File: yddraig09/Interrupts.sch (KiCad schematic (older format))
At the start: 0 parts

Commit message: More work on 6809 board
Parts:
- added C? (x6): 100nF, symbol Device:C
- added RN?: 10K, Resistor_THT:R_Array_SIP9, symbol Device:R_Network08
- added U? (x4): 74LS11, symbol 74xx:74LS11
- added U? (x10): 74LS32, symbol 74xx:74LS32
- added U?: 74LS147, symbol 74xx:74LS147
- added U?: 74LS540, symbol 74xx:74LS540
- added U?: 74LS574, symbol 74xx:74LS574
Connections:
- new net: U?.1, U?.11 (E1), U?.3
- new net: U?.13, U?.8
- new net: U?.2, U?.6
- new net: U?.12 (E2), U?.3, U?.6
- new net: U?.13 (E3), U?.4, U?.8
- new net: U?.1 (E4), U?.11, U?.5
- new net: U?.10, U?.3 (E6), U?.6
- new net: U?.11, U?.4 (E7), U?.8
- new net: U?.2 (E5), U?.3, U?.9
- new net: U?.19 (Q0), U?.2
- new net: U?.18 (Q1), U?.5
- new net: U?.10, U?.17 (Q2)
- new net: U?.13, U?.16 (Q3)
- new net: U?.15 (Q4), U?.2
- new net: U?.14 (Q5), U?.5
- new net: U?.10, U?.13 (Q6)
- new net: U?.11, U?.11 (Cp)
- new net: U?.14 (S3), U?.5 (A3)
- new net: U?.4 (A2), U?.6 (S2)
- new net: U?.3 (A1), U?.7 (S1)
- new net: U?.2 (A0), U?.9 (S0)
- new net +5V: C?.1, C?.1, C?.1, C?.1, C?.1, C?.1, RN?.1 (common), U?.10 (E9), U?.14 (VCC), U?.14 (VCC), U?.14 (VCC), U?.16 (VCC), U?.20 (VCC), U?.20 (VCC), U?.5 (E8), U?.6 (A4), U?.7 (A5), U?.8 (A6), U?.9 (A7)
- new net D0: U?.18 (Y0), U?.2 (D0)
- new net D1: U?.17 (Y1), U?.3 (D1)
- new net D2: U?.16 (Y2), U?.4 (D2)
- new net D3: U?.15 (Y3), U?.5 (D3)
- new net D4: U?.14 (Y4), U?.6 (D4)
- new net D5: U?.13 (Y5), U?.7 (D5)
- new net D6: U?.12 (Y6), U?.8 (D6)
- new net D7: U?.11 (Y7), U?.9 (D7)
- new net GND: C?.2, C?.2, C?.2, C?.2, C?.2, C?.2, U?.1 (OE), U?.10 (GND), U?.10 (GND), U?.7 (GND), U?.7 (GND), U?.7 (GND), U?.8 (GND)
- new net ~CS_IRQEN: U?.12, U?.19 (G2)
- new net ~IRQ: U?.12
- new net ~IRQ0: RN?.2 (R1), U?.1
- new net ~IRQ1: RN?.3 (R2), U?.4
- new net ~IRQ2: RN?.4 (R3), U?.9
- new net ~IRQ3: RN?.5 (R4), U?.12
- new net ~IRQ4: RN?.6 (R5), U?.1
- new net ~IRQ5: RN?.7 (R6), U?.4
- new net ~IRQ6: RN?.8 (R7), U?.9
- new net ~RD: U?.1 (G1)
- new net ~WR: U?.13
- no-connect marks 0 -> 2

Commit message: ddraig09: initial design done
Need to be reviewed and decode on additional uses for IO but passed DRC
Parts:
- added C801, C802, C803, C804, C805, C806: 100nF, symbol Device:C
- gave numbers to parts that had none: 13
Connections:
- net +5V: now also C801.1, C802.1, C803.1, C804.1, C805.1, C806.1
- net GND: now also C801.2, C802.2, C803.2, C804.2, C805.2, C806.2

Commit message: Asssigned part footprints to most of schematic
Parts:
- C801, C802, C803, C804, C805, C806, C807, C808, C809, C810, C811, C812: footprint (none) -> Capacitor_THT:C_Disc_D5.0mm_W2.5mm_P2.50mm
- U801, U803, U804: footprint (none) -> Package_DIP:DIP-14_W7.62mm_Socket
- U802, U806: footprint (none) -> Package_DIP:DIP-20_W7.62mm_Socket
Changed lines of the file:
@@
 F 0 "U804" H 9300 1450 50  0000 C CNN
 F 1 "74LS11" H 9700 1450 50  0000 C CNN
-F 2 "" H 9500 1200 50  0001 C CNN
+F 2 "Package_DIP:DIP-14_W7.62mm_Socket" H 9500 1200 50  0001 C CNN
 F 3 "http://www.ti.com/lit/gpn/sn74LS11" H 9500 1200 50  0001 C CNN
 	1    9500 1200
@@
 F 0 "U804" H 8350 1850 50  0000 C CNN
 F 1 "74LS11" H 8800 1850 50  0000 C CNN
-F 2 "" H 8550 1600 50  0001 C CNN
+F 2 "Package_DIP:DIP-14_W7.62mm_Socket" H 8550 1600 50  0001 C CNN
 F 3 "http://www.ti.com/lit/gpn/sn74LS11" H 8550 1600 50  0001 C CNN
 	2    8550 1600
@@
 F 0 "U804" H 8350 2400 50  0000 C CNN
 F 1 "74LS11" H 8800 2400 50  0000 C CNN
-F 2 "" H 8550 2150 50  0001 C CNN
+F 2 "Package_DIP:DIP-14_W7.62mm_Socket" H 8550 2150 50  0001 C CNN
 F 3 "http://www.ti.com/lit/gpn/sn74LS11" H 8550 2150 50  0001 C CNN
 	3    8550 2150
@@
 F 0 "U804" H 10700 6600 50  0000 L CNN
 F 1 "74LS11" H 10700 5900 50  0000 L CNN
-F 2 "" H 10650 6250 50  0001 C CNN
+F 2 "Package_DIP:DIP-14_W7.62mm_Socket" H 10650 6250 50  0001 C CNN
 F 3 "http://www.ti.com/lit/gpn/sn74LS11" H 10650 6250 50  0001 C CNN
 	4    10650 6250
@@
 F 0 "U801" H 5300 1750 50  0000 C CNN
 F 1 "74LS32" H 5700 1750 50  0000 C CNN
-F 2 "" H 5500 1500 50  0001 C CNN
+F 2 "Package_DIP:DIP-14_W7.62mm_Socket" H 5500 1500 50  0001 C CNN
 F 3 "http://www.ti.com/lit/gpn/sn74LS32" H 5500 1500 50  0001 C CNN
 	1    5500 1500
@@
 F 0 "U801" H 5300 2850 50  0000 C CNN
 F 1 "74LS32" H 5700 2850 50  0000 C CNN
-F 2 "" H 5500 2600 50  0001 C CNN
+F 2 "Package_DIP:DIP-14_W7.62mm_Socket" H 5500 2600 50  0001 C CNN
 F 3 "http://www.ti.com/lit/gpn/sn74LS32" H 5500 2600 50  0001 C CNN
 	3    5500 2600
@@
 F 0 "U803" H 5300 3400 50  0000 C CNN
 F 1 "74LS32" H 5700 3400 50  0000 C CNN
-F 2 "" H 5500 3150 50  0001 C CNN
+F 2 "Package_DIP:DIP-14_W7.62mm_Socket" H 5500 3150 50  0001 C CNN
 F 3 "http://www.ti.com/lit/gpn/sn74LS32" H 5500 3150 50  0001 C CNN
 	4    5500 3150
@@
 F 0 "U803" H 10050 6600 50  0000 L CNN
 F 1 "74LS32" H 10050 5900 50  0000 L CNN
-F 2 "" H 10000 6250 50  0001 C CNN
+F 2 "Package_DIP:DIP-14_W7.62mm_Socket" H 10000 6250 50  0001 C CNN
 F 3 "http://www.ti.com/lit/gpn/sn74LS32" H 10000 6250 50  0001 C CNN
 	5    10000 6250
@@
 F 0 "U803" H 5300 4000 50  0000 C CNN
 F 1 "74LS32" H 5700 4000 50  0000 C CNN
-F 2 "" H 5500 3750 50  0001 C CNN
+F 2 "Package_DIP:DIP-14_W7.62mm_Socket" H 5500 3750 50  0001 C CNN
 F 3 "http://www.ti.com/lit/gpn/sn74LS32" H 5500 3750 50  0001 C CNN
 	1    5500 3750
@@
 F 0 "U803" H 5300 4550 50  0000 C CNN
 F 1 "74LS32" H 5700 4550 50  0000 C CNN
-F 2 "" H 5500 4300 50  0001 C CNN
+F 2 "Package_DIP:DIP-14_W7.62mm_Socket" H 5500 4300 50  0001 C CNN
 F 3 "http://www.ti.com/lit/gpn/sn74LS32" H 5500 4300 50  0001 C CNN
 	2    5500 4300
@@
 F 0 "U803" H 5300 5100 50  0000 C CNN
 F 1 "74LS32" H 5700 5100 50  0000 C CNN
-F 2 "" H 5500 4850 50  0001 C CNN
+F 2 "Package_DIP:DIP-14_W7.62mm_Socket" H 5500 4850 50  0001 C CNN
 F 3 "http://www.ti.com/lit/gpn/sn74LS32" H 5500 4850 50  0001 C CNN
 	3    5500 4850
@@
 F 0 "U801" H 1850 6950 50  0000 C CNN
 F 1 "74LS32" H 2100 6500 50  0000 C CNN
-F 2 "" H 2050 6700 50  0001 C CNN
+F 2 "Package_DIP:DIP-14_W7.62mm_Socket" H 2050 6700 50  0001 C CNN
 F 3 "http://www.ti.com/lit/gpn/sn74LS32" H 2050 6700 50  0001 C CNN
 	4    2050 6700
@@
 F 0 "U801" H 9400 6600 50  0000 L CNN
 F 1 "74LS32" H 9400 5900 50  0000 L CNN
-F 2 "" H 9350 6250 50  0001 C CNN
+F 2 "Package_DIP:DIP-14_W7.62mm_Socket" H 9350 6250 50  0001 C CNN
 F 3 "http://www.ti.com/lit/gpn/sn74LS32" H 9350 6250 50  0001 C CNN
 	5    9350 6250
@@
 F 0 "U806" H 9650 4400 50  0000 C CNN
 F 1 "74LS540" H 10100 4400 50  0000 C CNN
-F 2 "" H 9900 3750 50  0001 C CNN
+F 2 "Package_DIP:DIP-20_W7.62mm_Socket" H 9900 3750 50  0001 C CNN
 F 3 "http://www.ti.com/lit/gpn/sn74LS540" H 9900 3750 50  0001 C CNN
 	1    9900 3750
@@
 F 0 "U802" H 3250 6950 50  0000 C CNN
 F 1 "74LS574" H 3700 6950 50  0000 C CNN
-F 2 "" H 3500 6300 50  0001 C CNN
+F 2 "Package_DIP:DIP-20_W7.62mm_Socket" H 3500 6300 50  0001 C CNN
 F 3 "http://www.ti.com/lit/gpn/sn74LS574" H 3500 6300 50  0001 C CNN
 	1    3500 6300
@@
 F 0 "U801" H 5300 2300 50  0000 C CNN
 F 1 "74LS32" H 5700 2300 50  0000 C CNN
-F 2 "" H 5500 2050 50  0001 C CNN
+F 2 "Package_DIP:DIP-14_W7.62mm_Socket" H 5500 2050 50  0001 C CNN
 F 3 "http://www.ti.com/lit/gpn/sn74LS32" H 5500 2050 50  0001 C CNN
 	2    5500 2050
@@
 F 0 "C807" H 6265 6296 50  0000 L CNN
 F 1 "100nF" H 6265 6205 50  0000 L CNN
-F 2 "" H 6188 6100 50  0001 C CNN
+F 2 "Capacitor_THT:C_Disc_D5.0mm_W2.5mm_P2.50mm" H 6188 6100 50  0001 C CNN
 F 3 "~" H 6150 6250 50  0001 C CNN
 	1    6150 6250
@@
 F 0 "C808" H 6765 6296 50  0000 L CNN
 F 1 "100nF" H 6765 6205 50  0000 L CNN
-F 2 "" H 6688 6100 50  0001 C CNN
+F 2 "Capacitor_THT:C_Disc_D5.0mm_W2.5mm_P2.50mm" H 6688 6100 50  0001 C CNN
 F 3 "~" H 6650 6250 50  0001 C CNN
 	1    6650 6250
@@
 F 0 "C809" H 7265 6296 50  0000 L CNN
 F 1 "100nF" H 7265 6205 50  0000 L CNN
-F 2 "" H 7188 6100 50  0001 C CNN
+F 2 "Capacitor_THT:C_Disc_D5.0mm_W2.5mm_P2.50mm" H 7188 6100 50  0001 C CNN
 F 3 "~" H 7150 6250 50  0001 C CNN
 	1    7150 6250
@@
 F 0 "C810" H 7765 6296 50  0000 L CNN
 F 1 "100nF" H 7765 6205 50  0000 L CNN
-F 2 "" H 7688 6100 50  0001 C CNN
+F 2 "Capacitor_THT:C_Disc_D5.0mm_W2.5mm_P2.50mm" H 7688 6100 50  0001 C CNN
 F 3 "~" H 7650 6250 50  0001 C CNN
 	1    7650 6250
@@
 F 0 "C811" H 8265 6296 50  0000 L CNN
 F 1 "100nF" H 8265 6205 50  0000 L CNN
-F 2 "" H 8188 6100 50  0001 C CNN
+F 2 "Capacitor_THT:C_Disc_D5.0mm_W2.5mm_P2.50mm" H 8188 6100 50  0001 C CNN
 F 3 "~" H 8150 6250 50  0001 C CNN
 	1    8150 6250
@@
 F 0 "C812" H 8765 6296 50  0000 L CNN
 F 1 "100nF" H 8765 6205 50  0000 L CNN
-F 2 "" H 8688 6100 50  0001 C CNN
+F 2 "Capacitor_THT:C_Disc_D5.0mm_W2.5mm_P2.50mm" H 8688 6100 50  0001 C CNN
 F 3 "~" H 8650 6250 50  0001 C CNN
 	1    8650 6250
@@
 F 0 "C801" H 1565 3246 50  0000 L CNN
 F 1 "100nF" H 1565 3155 50  0000 L CNN
-F 2 "" H 1488 3050 50  0001 C CNN
+F 2 "Capacitor_THT:C_Disc_D5.0mm_W2.5mm_P2.50mm" H 1488 3050 50  0001 C CNN
 F 3 "~" H 1450 3200 50  0001 C CNN
 	1    1450 3200
@@
 F 0 "C802" H 2065 3246 50  0000 L CNN
 F 1 "100nF" H 2065 3155 50  0000 L CNN
-F 2 "" H 1988 3050 50  0001 C CNN
+F 2 "Capacitor_THT:C_Disc_D5.0mm_W2.5mm_P2.50mm" H 1988 3050 50  0001 C CNN
 F 3 "~" H 1950 3200 50  0001 C CNN
 	1    1950 3200
@@
 F 0 "C804" H 2565 3246 50  0000 L CNN
 F 1 "100nF" H 2565 3155 50  0000 L CNN
-F 2 "" H 2488 3050 50  0001 C CNN
+F 2 "Capacitor_THT:C_Disc_D5.0mm_W2.5mm_P2.50mm" H 2488 3050 50  0001 C CNN
 F 3 "~" H 2450 3200 50  0001 C CNN
 	1    2450 3200
@@
 F 0 "C806" H 3065 3246 50  0000 L CNN
 F 1 "100nF" H 3065 3155 50  0000 L CNN
-F 2 "" H 2988 3050 50  0001 C CNN
+F 2 "Capacitor_THT:C_Disc_D5.0mm_W2.5mm_P2.50mm" H 2988 3050 50  0001 C CNN
 F 3 "~" H 2950 3200 50  0001 C CNN
 	1    2950 3200
@@
 F 0 "C803" H 2065 4396 50  0000 L CNN
 F 1 "100nF" H 2065 4305 50  0000 L CNN
-F 2 "" H 1988 4200 50  0001 C CNN
+F 2 "Capacitor_THT:C_Disc_D5.0mm_W2.5mm_P2.50mm" H 1988 4200 50  0001 C CNN
 F 3 "~" H 1950 4350 50  0001 C CNN
 	1    1950 4350
@@
 F 0 "C805" H 2565 4396 50  0000 L CNN
 F 1 "100nF" H 2565 4305 50  0000 L CNN
-F 2 "" H 2488 4200 50  0001 C CNN
+F 2 "Capacitor_THT:C_Disc_D5.0mm_W2.5mm_P2.50mm" H 2488 4200 50  0001 C CNN
 F 3 "~" H 2450 4350 50  0001 C CNN
 	1    2450 4350

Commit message: ddraig09: all footprints assigned
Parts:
- U805: footprint (none) -> Package_DIP:DIP-16_W7.62mm_Socket
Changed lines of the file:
@@
 F 0 "U805" H 8300 4200 50  0000 C CNN
 F 1 "74LS147" H 8750 4200 50  0000 C CNN
-F 2 "" H 8550 3650 50  0001 C CNN
+F 2 "Package_DIP:DIP-16_W7.62mm_Socket" H 8550 3650 50  0001 C CNN
 F 3 "http://www.ti.com/lit/gpn/sn74LS147" H 8550 3650 50  0001 C CNN
 	1    8550 3650

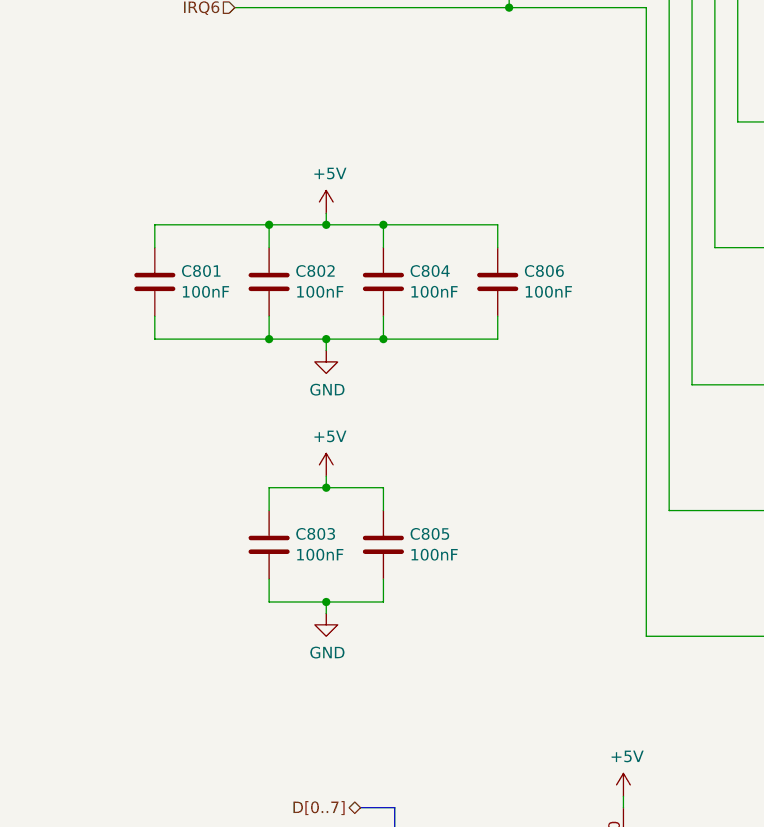
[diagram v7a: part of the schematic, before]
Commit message: Added initial 6809 board layout design
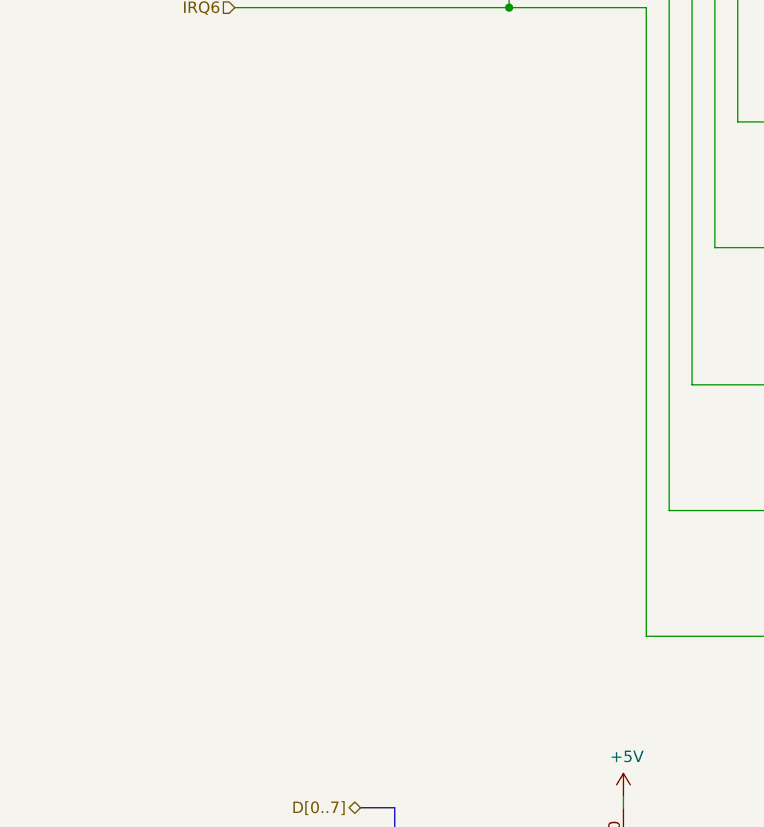
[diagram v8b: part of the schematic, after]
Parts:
- removed C801, C802, C803, C804, C805, C806: 100nF, Capacitor_THT:C_Disc_D5.0mm_W2.5mm_P2.50mm, symbol Device:C
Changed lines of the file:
@@
 Wire Bus Line
 	6950 4950 10850 4950
-$Comp
-L Device:C C801
-U 1 1 616F4D00
-P 1450 3200
-F 0 "C801" H 1565 3246 50  0000 L CNN
-F 1 "100nF" H 1565 3155 50  0000 L CNN
-F 2 "Capacitor_THT:C_Disc_D5.0mm_W2.5mm_P2.50mm" H 1488 3050 50  0001 C CNN
-F 3 "~" H 1450 3200 50  0001 C CNN
-	1    1450 3200
-	1    0    0    -1
-$EndComp
-$Comp
-L Device:C C802
-U 1 1 616F4D06
-P 1950 3200
-F 0 "C802" H 2065 3246 50  0000 L CNN
-F 1 "100nF" H 2065 3155 50  0000 L CNN
-F 2 "Capacitor_THT:C_Disc_D5.0mm_W2.5mm_P2.50mm" H 1988 3050 50  0001 C CNN
-F 3 "~" H 1950 3200 50  0001 C CNN
-	1    1950 3200
-	1    0    0    -1
-$EndComp
-$Comp
-L Device:C C804
-U 1 1 616F4D0C
-P 2450 3200
-F 0 "C804" H 2565 3246 50  0000 L CNN
-F 1 "100nF" H 2565 3155 50  0000 L CNN
-F 2 "Capacitor_THT:C_Disc_D5.0mm_W2.5mm_P2.50mm" H 2488 3050 50  0001 C CNN
-F 3 "~" H 2450 3200 50  0001 C CNN
-	1    2450 3200
-	1    0    0    -1
-$EndComp
-$Comp
-L Device:C C806
-U 1 1 616F4D12
-P 2950 3200
-F 0 "C806" H 3065 3246 50  0000 L CNN
-F 1 "100nF" H 3065 3155 50  0000 L CNN
-F 2 "Capacitor_THT:C_Disc_D5.0mm_W2.5mm_P2.50mm" H 2988 3050 50  0001 C CNN
-F 3 "~" H 2950 3200 50  0001 C CNN
-	1    2950 3200
-	1    0    0    -1
-$EndComp
-$Comp
-L power:+5V #PWR0801
-U 1 1 616F4D18
-P 2200 2900
-F 0 "#PWR0801" H 2200 2750 50  0001 C CNN
-F 1 "+5V" H 2215 3073 50  0000 C CNN
-F 2 "" H 2200 2900 50  0001 C CNN
-F 3 "" H 2200 2900 50  0001 C CNN
-	1    2200 2900
-	1    0    0    -1
-$EndComp
-$Comp
-L power:GND #PWR0802
-U 1 1 616F4D1E
-P 2200 3500
-F 0 "#PWR0802" H 2200 3250 50  0001 C CNN
-F 1 "GND" H 2205 3327 50  0000 C CNN
-F 2 "" H 2200 3500 50  0001 C CNN
-F 3 "" H 2200 3500 50  0001 C CNN
-	1    2200 3500
-	1    0    0    -1
-$EndComp
-Wire Wire Line
-	1450 3050 1450 2950
-Wire Wire Line
-	1450 2950 1950 2950
-Wire Wire Line
-	2950 2950 2950 3050
-Connection ~ 2200 2950
-Wire Wire Line
-	2200 2950 2450 2950
-Wire Wire Line
-	2200 2900 2200 2950
-Wire Wire Line
-	1450 3350 1450 3450
-Wire Wire Line
-	1450 3450 1950 3450
-Wire Wire Line
-	2950 3450 2950 3350
-Wire Wire Line
-	2200 3500 2200 3450
-Connection ~ 2200 3450
-Wire Wire Line
-	2200 3450 2450 3450
-Wire Wire Line
-	1950 3350 1950 3450
-Connection ~ 1950 3450
-Wire Wire Line
-	1950 3450 2200 3450
-Wire Wire Line
-	1950 3050 1950 2950
-Connection ~ 1950 2950
-Wire Wire Line
-	1950 2950 2200 2950
-Wire Wire Line
-	2450 3050 2450 2950
-Connection ~ 2450 2950
-Wire Wire Line
-	2450 2950 2950 2950
-Wire Wire Line
-	2450 3350 2450 3450
-Connection ~ 2450 3450
-Wire Wire Line
-	2450 3450 2950 3450
-$Comp
-L Device:C C803
-U 1 1 61703ED0
-P 1950 4350
-F 0 "C803" H 2065 4396 50  0000 L CNN
-F 1 "100nF" H 2065 4305 50  0000 L CNN
-F 2 "Capacitor_THT:C_Disc_D5.0mm_W2.5mm_P2.50mm" H 1988 4200 50  0001 C CNN
-F 3 "~" H 1950 4350 50  0001 C CNN
-	1    1950 4350
-	1    0    0    -1
-$EndComp
-$Comp
-L Device:C C805
-U 1 1 61703ED6
-P 2450 4350
-F 0 "C805" H 2565 4396 50  0000 L CNN
-F 1 "100nF" H 2565 4305 50  0000 L CNN
-F 2 "Capacitor_THT:C_Disc_D5.0mm_W2.5mm_P2.50mm" H 2488 4200 50  0001 C CNN
-F 3 "~" H 2450 4350 50  0001 C CNN
-	1    2450 4350
-	1    0    0    -1
-$EndComp
-$Comp
-L power:+5V #PWR0803
-U 1 1 61703EE2
-P 2200 4050
-F 0 "#PWR0803" H 2200 3900 50  0001 C CNN
-F 1 "+5V" H 2215 4223 50  0000 C CNN
-F 2 "" H 2200 4050 50  0001 C CNN
-F 3 "" H 2200 4050 50  0001 C CNN
-	1    2200 4050
-	1    0    0    -1
-$EndComp
-$Comp
-L power:GND #PWR0804
-U 1 1 61703EE8
-P 2200 4650
-F 0 "#PWR0804" H 2200 4400 50  0001 C CNN
-F 1 "GND" H 2205 4477 50  0000 C CNN
-F 2 "" H 2200 4650 50  0001 C CNN
-F 3 "" H 2200 4650 50  0001 C CNN
-	1    2200 4650
-	1    0    0    -1
-$EndComp
-Connection ~ 2200 4100
-Wire Wire Line
-	2200 4100 2450 4100
-Wire Wire Line
-	2200 4050 2200 4100
-Wire Wire Line
-	2200 4650 2200 4600
-Connection ~ 2200 4600
-Wire Wire Line
-	2200 4600 2450 4600
-Wire Wire Line
-	1950 4500 1950 4600
-Wire Wire Line
-	1950 4600 2200 4600
-Wire Wire Line
-	1950 4200 1950 4100
-Wire Wire Line
-	1950 4100 2200 4100
-Wire Wire Line
-	2450 4200 2450 4100
-Wire Wire Line
-	2450 4500 2450 4600
 Wire Bus Line
 	10850 3350 10850 4950
